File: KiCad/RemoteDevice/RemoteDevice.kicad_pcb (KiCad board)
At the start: 2 copper layers, 93 x 52.5 mm, 42 parts, among them J1 CN1, J2 Antenne, Q1 Si4435, SW1 BP, SW2 BP, U1 STM32L041F6Px, U2 XC9140, U3 MCP6281, U4 ADT7410TRZ, U5 MCP6281, U6 RT606, U7 Microphone

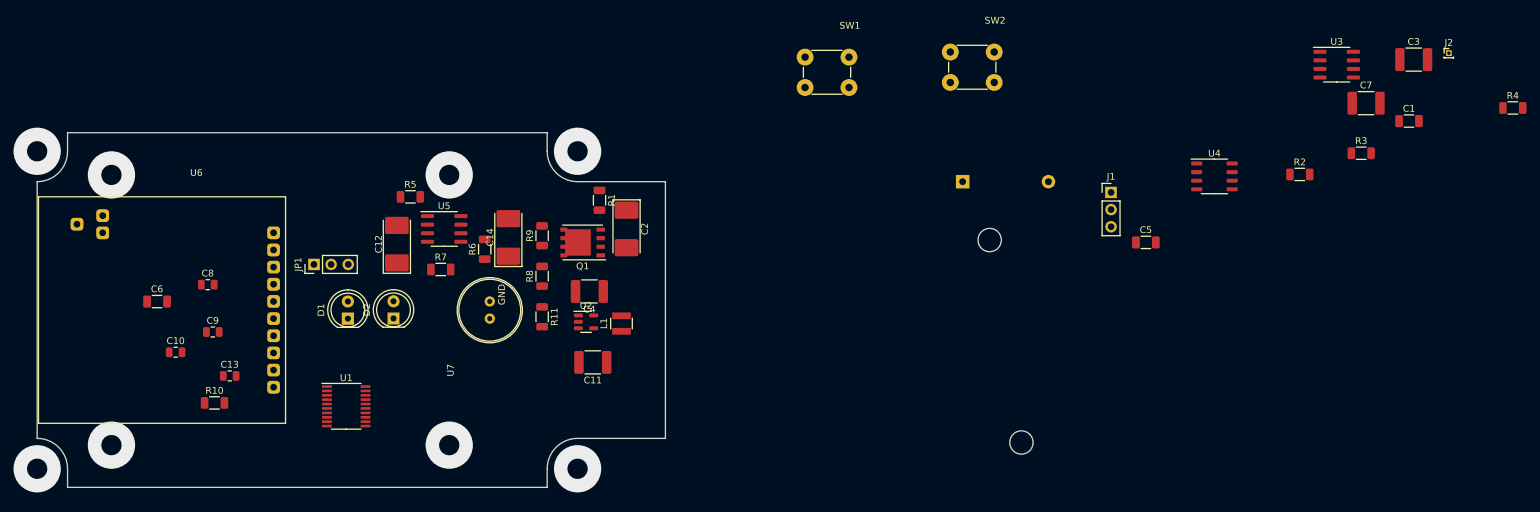
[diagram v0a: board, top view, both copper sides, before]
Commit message: routage bien avancé. Vérifier remap harmoniser odt. Reprendre pack RT606 pour passer cuivre entre pastille
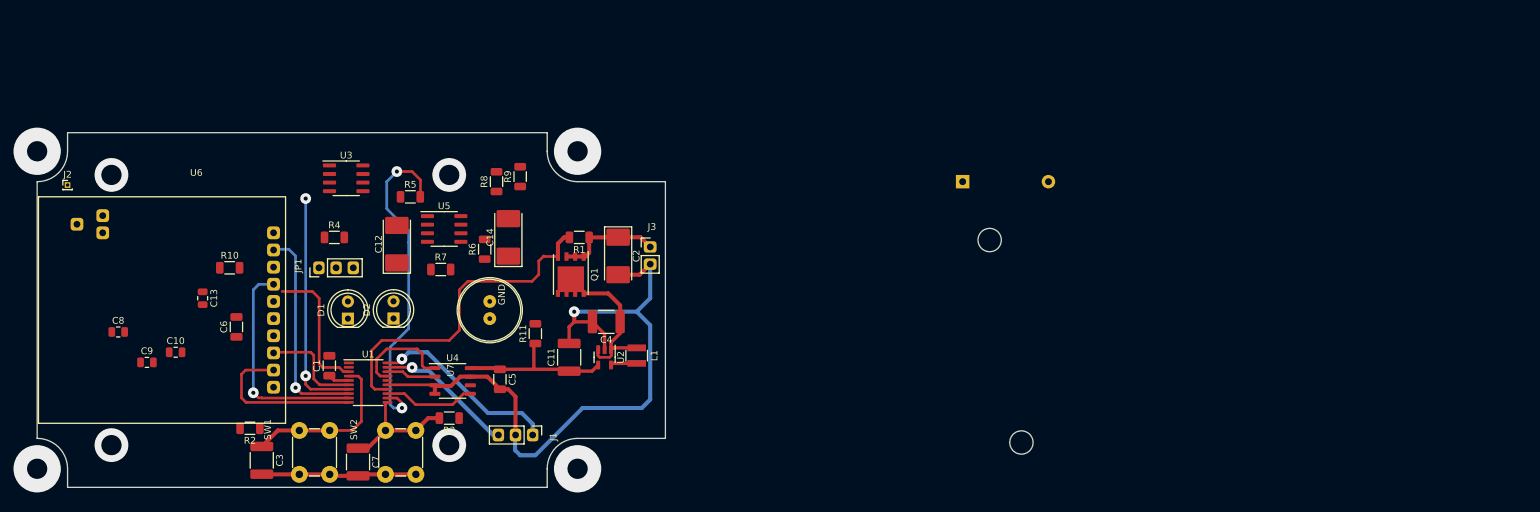
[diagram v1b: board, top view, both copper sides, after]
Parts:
- added J3: Alim, LibKiCad_PjtDeviceManagePV:PinHeader2pts, F.Cu at (118.8, 82.3)
- J1, JP1: footprint Connector_PinHeader_2.54mm:PinHeader_1x03_P2.54mm_Vertical -> LibKiCad_PjtDeviceManagePV:PinHeader3pts
- moved J2 205.4 mm to (32.5, 70.5)
- moved C3 180.5 mm to (61.2, 111.2), turned to -90 degrees
- moved R4 175.5 mm to (72.0, 78.2)
- moved C1 163.9 mm to (71.2, 97.2), turned to 90 degrees
- moved R2 159.9 mm to (59.5, 106.5), turned to 180 degrees
- moved C7 158.4 mm to (75.5, 111.5), turned to -90 degrees
- moved U3 147.6 mm to (73.8, 69.5)
- moved R3 140.6 mm to (89.0, 105.0), turned to 180 degrees
- moved U4 116.8 mm to (89.5, 99.5)
- moved SW2 102.1 mm to (81.8, 110.0), turned to 90 degrees
- moved C5 97.7 mm to (96.5, 99.2), turned to -90 degrees
- moved J1 95.2 mm to (98.8, 107.5), turned to -90 degrees
- moved SW1 94.6 mm to (69.0, 110.0), turned to 90 degrees
- moved R10 20.1 mm to (56.5, 82.8)
- moved R8 15.5 mm to (96.0, 70.0)
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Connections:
- BT1 pad 1: +3V0 -> unconnected-(BT1-Pad1)
- BT1 pad 2: GND -> unconnected-(BT1-Pad2)
- U1 pad 10: /MicroPhone -> /RxCmde
- U1 pad 11: /RxCmde -> /UserBP
- U1 pad 12: /TxCmde -> /MicroPhone
- U1 pad 13: /CarrierDetect -> /INT
- U1 pad 14: /UserBP -> /BoostEn
- U1 pad 3: /INT -> /CarrierDetect
- U1 pad 6: /BoostEn -> /TxCmde
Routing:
- net GND: track 0.00 -> 125.9 mm, vias 0 -> 1
- net /BoostEn: track 0.00 -> 49.9 mm
- net /MicroPhone: track 0.00 -> 49.3 mm, vias 0 -> 2
- net /CmdeLED_IR: track 0.00 -> 34.2 mm, vias 0 -> 2
- net /DataOut: track 0.00 -> 33.0 mm, vias 0 -> 1
- net /DataIn: track 0.00 -> 31.6 mm, vias 0 -> 1
- net /SWCLK: track 0.00 -> 28.2 mm, vias 0 -> 1
- net /RxCmde: track 0.00 -> 24.7 mm
- net /Reset: track 0.00 -> 24.6 mm
- net +5V: track 0.00 -> 23.4 mm
- net /Vbatt: track 0.00 -> 21.7 mm
- net /SWDIO: track 0.00 -> 20.6 mm, vias 0 -> 1
- net /CarrierDetect: track 0.00 -> 20.5 mm
- net +3V0: track 0.00 -> 18.7 mm
- net /UserBP: track 0.00 -> 18.2 mm
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
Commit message: paxkagez RT606 OK, remap à contrôler, routage presque entièrement dégrossi, pb DRC sur edge cut
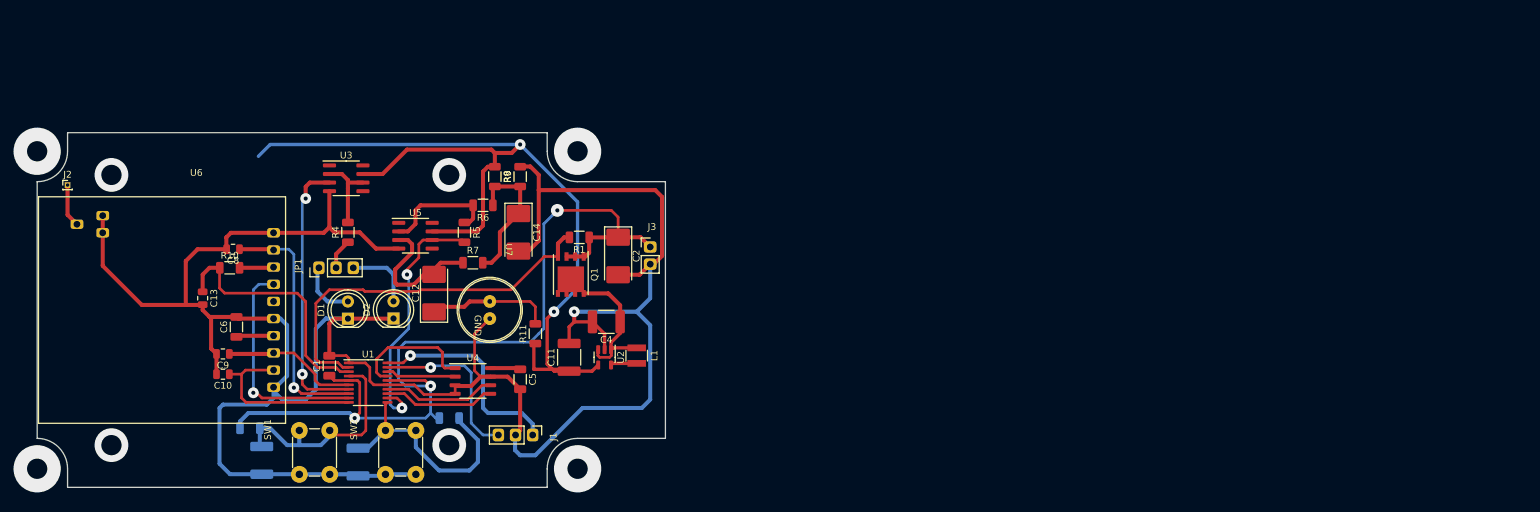
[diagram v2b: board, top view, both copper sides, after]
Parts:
- removed BT1: Battery 3V, Battery:BatteryHolder_Keystone_2468_2xAAA
- C3, C7, R2, R3: moved to B.Cu
- moved C8 21.0 mm to (57.0, 80.0), turned to 180 degrees
- moved C9 11.3 mm to (55.5, 95.5), turned to 180 degrees
- moved R5 9.57 mm to (91.2, 77.5), turned to -90 degrees
- moved C12 9.10 mm to (86.8, 86.5)
- moved C10 7.72 mm to (55.5, 98.5), turned to 180 degrees
- moved R6 6.50 mm to (94.0, 73.5), turned to 180 degrees
- moved R7 4.85 mm to (92.5, 82.0)
- moved U5 4.37 mm to (84.0, 78.0)
- moved C5 3.00 mm to (99.5, 99.2)
- moved U4 3.00 mm to (92.5, 99.5)
- moved R4 2.14 mm to (74.0, 77.5), turned to 90 degrees
- moved C14 1.68 mm to (99.2, 77.5), turned to -90 degrees
- moved R8 0.79 mm to (95.8, 69.2), turned to -90 degrees
- turned R2 to 0 degrees
- turned R3 to 0 degrees
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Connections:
- U1 pad 14: /BoostEn -> /CT
- U1 pad 2: /CT -> /BoostEn
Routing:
- net GND: track 125.9 -> 364.4 mm
- net +5V: track 23.4 -> 150.4 mm, vias 0 -> 2
- net +3V0: track 18.7 -> 131.8 mm, vias 0 -> 3
- net /VtGND: track 0.00 -> 22.8 mm
- net /MIC_InAOP: track 0.00 -> 20.2 mm
- net /MiC: track 0.00 -> 18.2 mm
- net /CR_AOP: track 0.00 -> 17.3 mm
- net /UserBP: track 18.2 -> 35.2 mm
- net /CarrierDetect: track 20.5 -> 37.5 mm
- net /CT: track 0.00 -> 16.8 mm
- net /Out_LED: track 0.00 -> 11.7 mm
- net /MicroPhone: track 49.3 -> 38.8 mm
- net /LED_Side: track 0.00 -> 10.3 mm
- net /Reset: track 24.6 -> 34.0 mm
- net /LED_Top: track 0.00 -> 8.70 mm
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
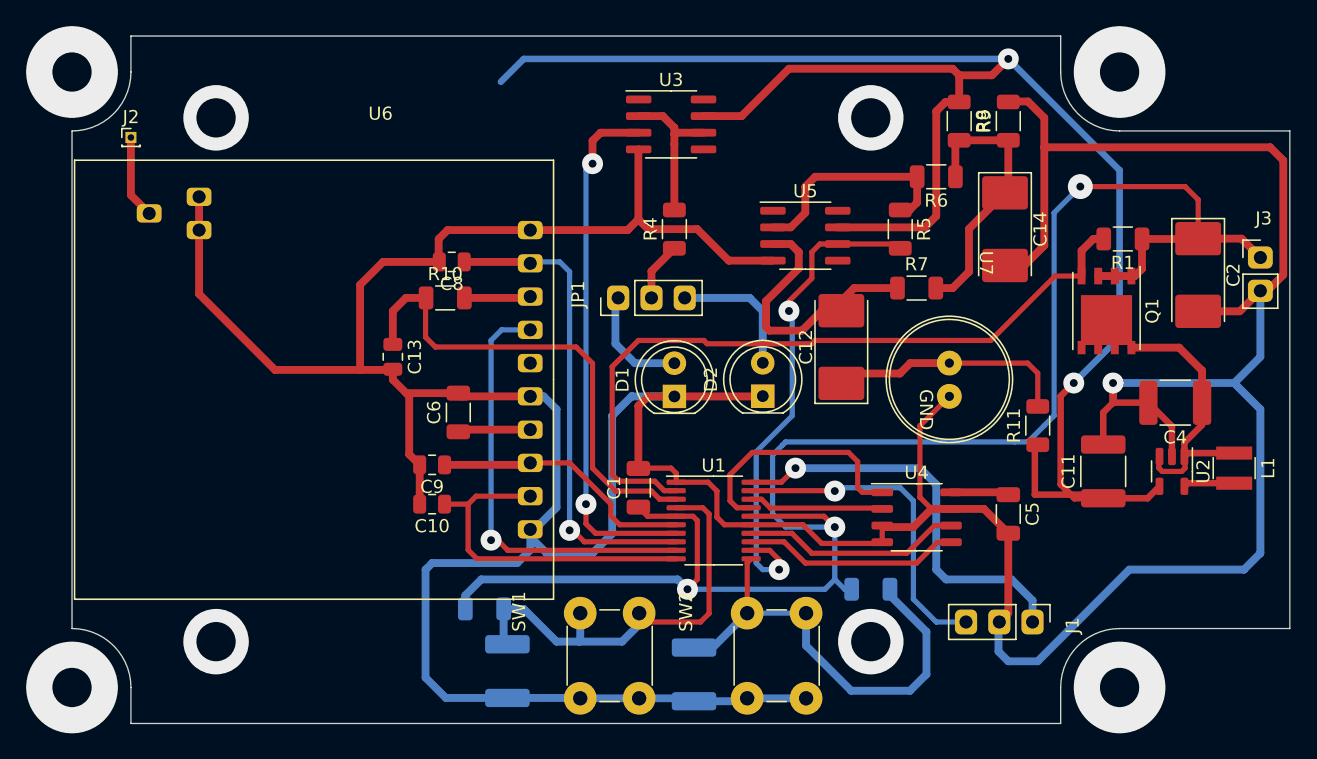
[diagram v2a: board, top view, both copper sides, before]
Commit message: Routage très avancé, pb edge cut réglé, remap à vérifier, silkscreen OK sur cmp name
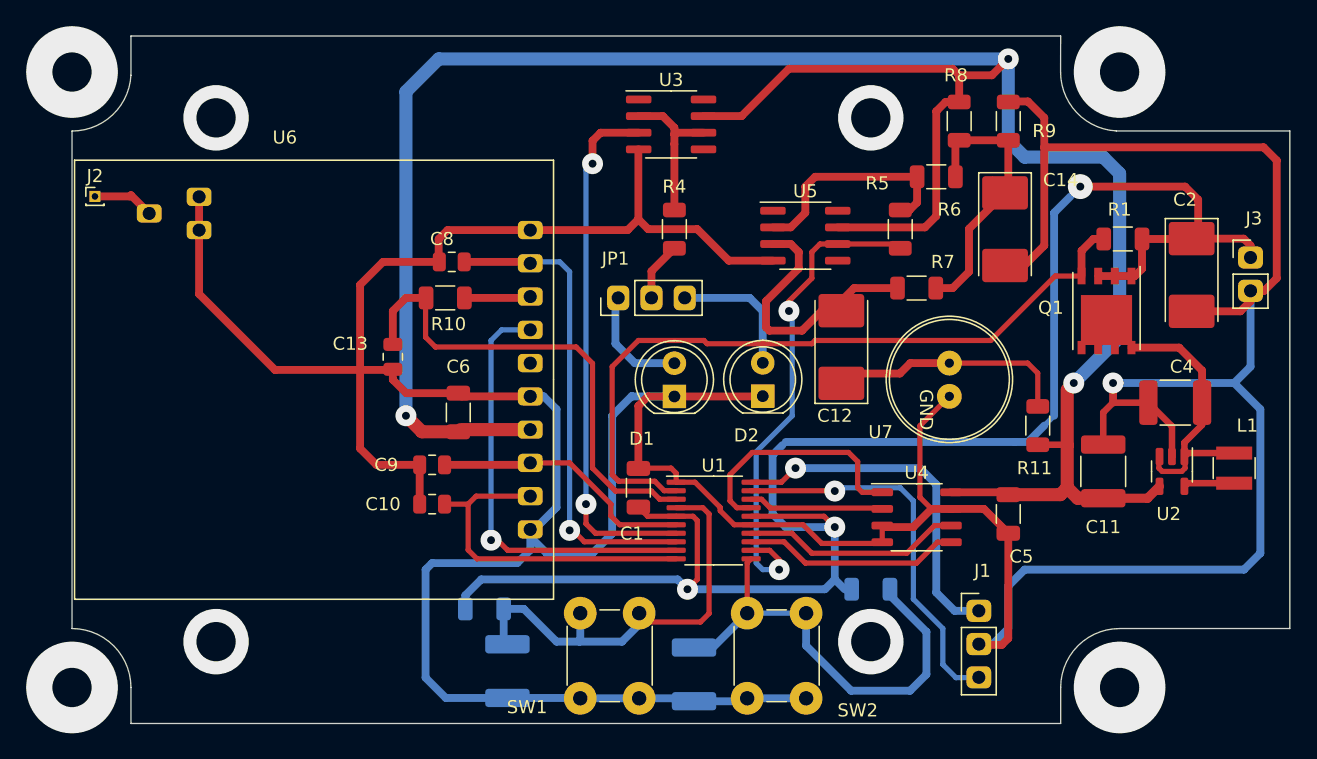
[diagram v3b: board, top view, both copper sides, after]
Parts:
- moved J2 5.27 mm to (29.8, 75.0)
- moved J1 2.30 mm to (97.2, 109.2), turned to 0 degrees
- moved J3 0.75 mm to (118.0, 82.3)
- moved C2 0.50 mm to (113.5, 81.0)
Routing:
- net +5V: track 150.4 -> 188.7 mm, vias 2 -> 3
- net GND: track 364.4 -> 371.5 mm
- net /SWCLK: track 31.6 -> 27.2 mm
- net /SWDIO: track 25.2 -> 29.5 mm
- net /Ant: track 6.38 -> 4.76 mm
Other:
- outline, holes or cut-outs redrawn

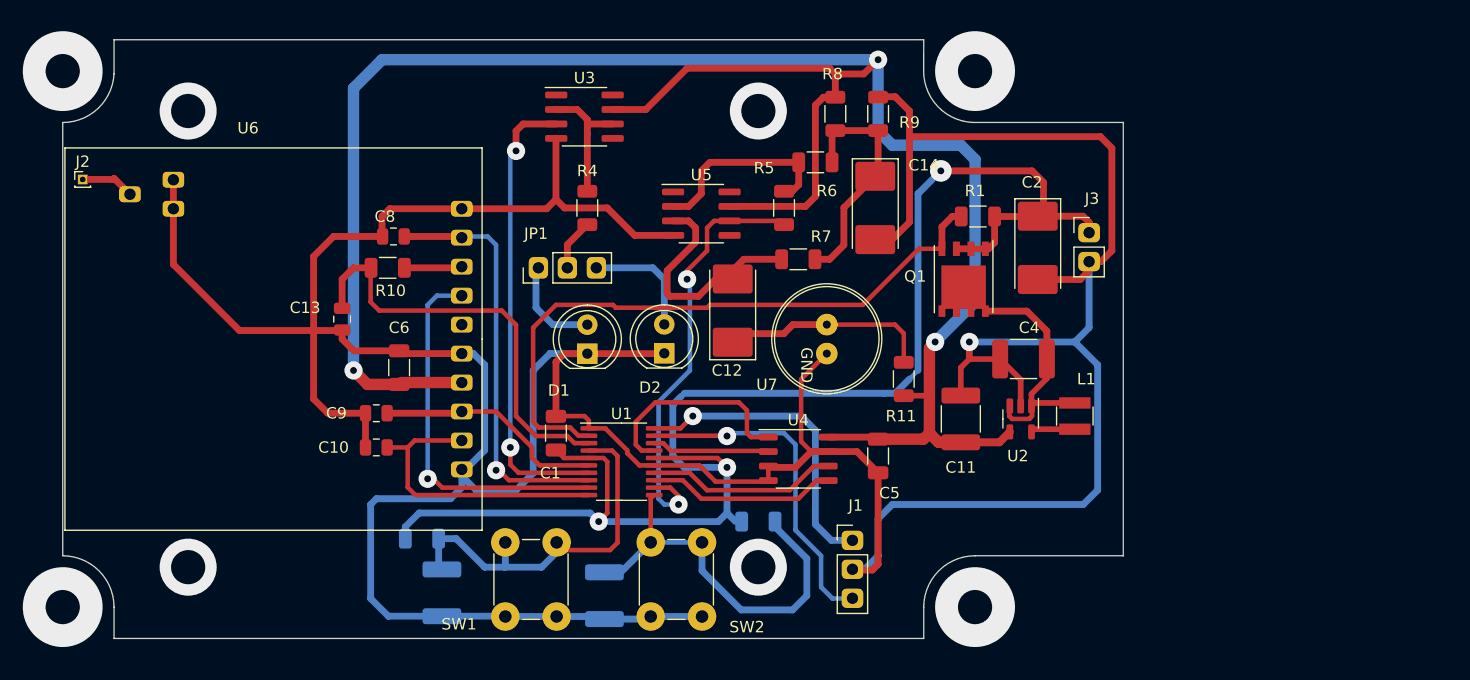
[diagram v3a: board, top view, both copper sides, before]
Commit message: suppression des warning et erreurs, il en reste mais pas grave. Vérifier remap
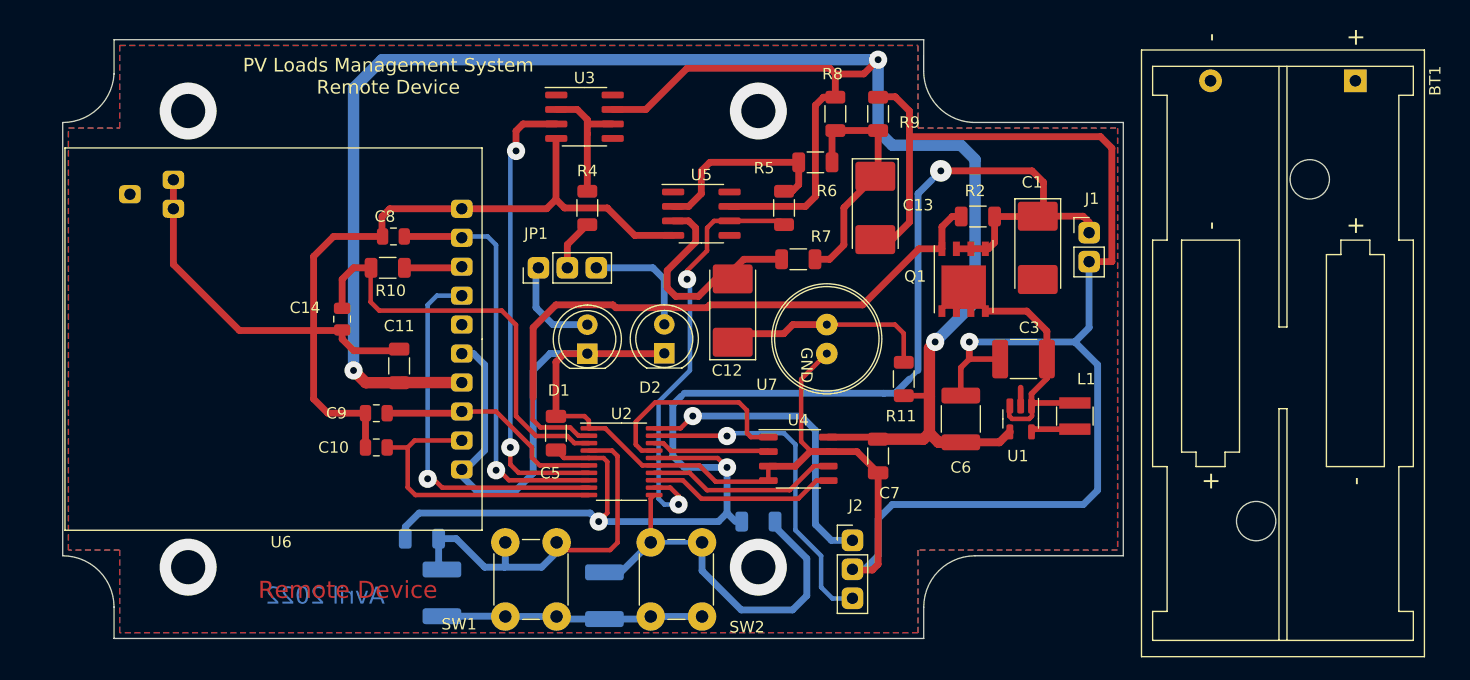
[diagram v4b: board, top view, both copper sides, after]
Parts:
- removed the J2 at (29.8, 75.0)
- added BT1: Battery 3V, Battery:BatteryHolder_Keystone_2468_2xAAA, F.Cu at (141.3, 66.3)
- moved C11 0.15 mm to (57.5, 91.3)
- renumbered C2 to C1, C6 to C11, C14 to C13, C13 to C14, C3 to C2, C4 to C3, C7 to C4, C1 to C5, C11 to C6, C5 to C7, J3 to J1, J1 to J2, R2 to R1, R1 to R2, U2 to U1, U1 to U2
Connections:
- U6 pad 11: /Ant -> unconnected-(U6-Pad11)
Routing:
- net GND: track 371.5 -> 332.6 mm
- net /Ant: track 4.76 -> 0.00 mm
- net /VtGND: track 22.8 -> 21.0 mm
- net +5V: track 188.7 -> 187.9 mm
- net (no net): vias 8 -> 4
- added copper zone on B.Cu, net GND
- added copper zone on F.Cu, net GND
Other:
- board text added: "Avril 2022"
- board text added: "PV Loads Management System Remote Device"
- board text added: "Remote Device"
